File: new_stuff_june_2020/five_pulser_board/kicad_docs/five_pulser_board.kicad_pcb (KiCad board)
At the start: 2 copper layers, 39.4 x 78.7 mm, 49 parts, among them J1 signal_in, J2 CV_in, J3 Conn_02x05_Odd_Even, J4 signal_out, J5 pulses, U1 TL072, U2 LM3914, U3 TL072

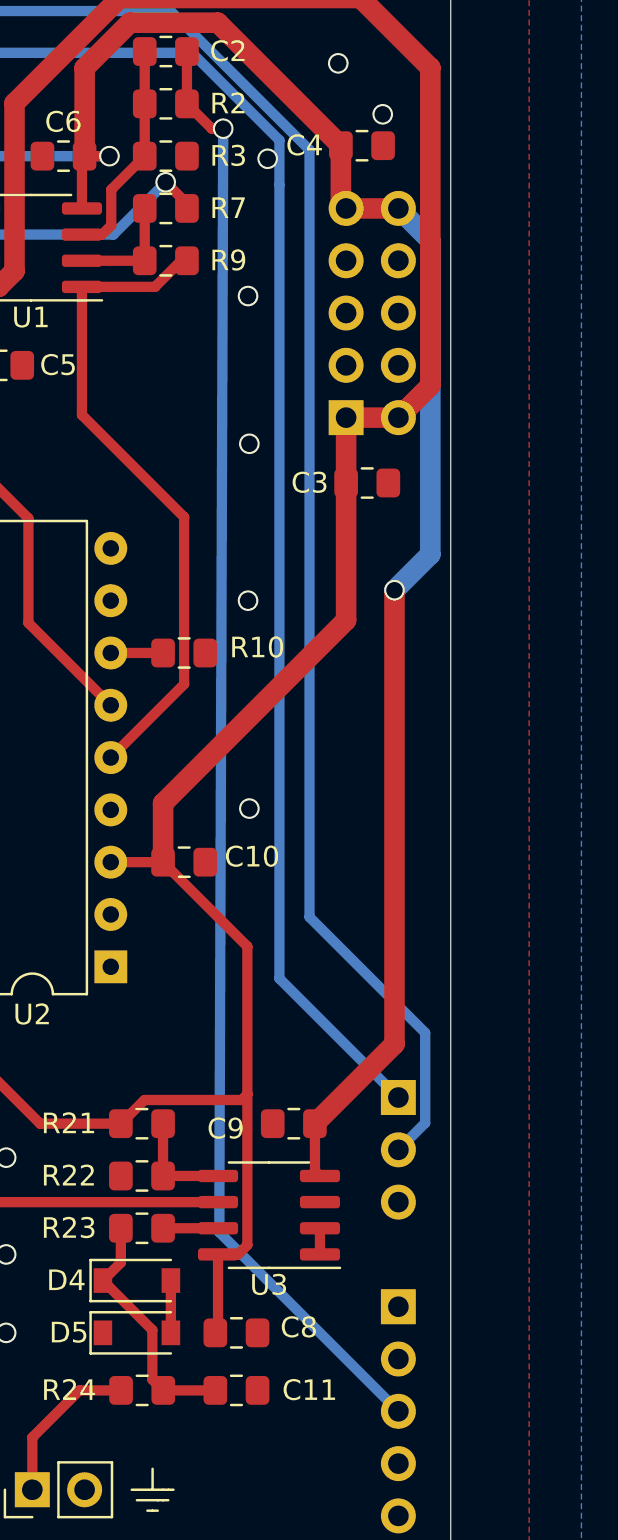
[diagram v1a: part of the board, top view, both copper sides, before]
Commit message: fix pcb error, change some values
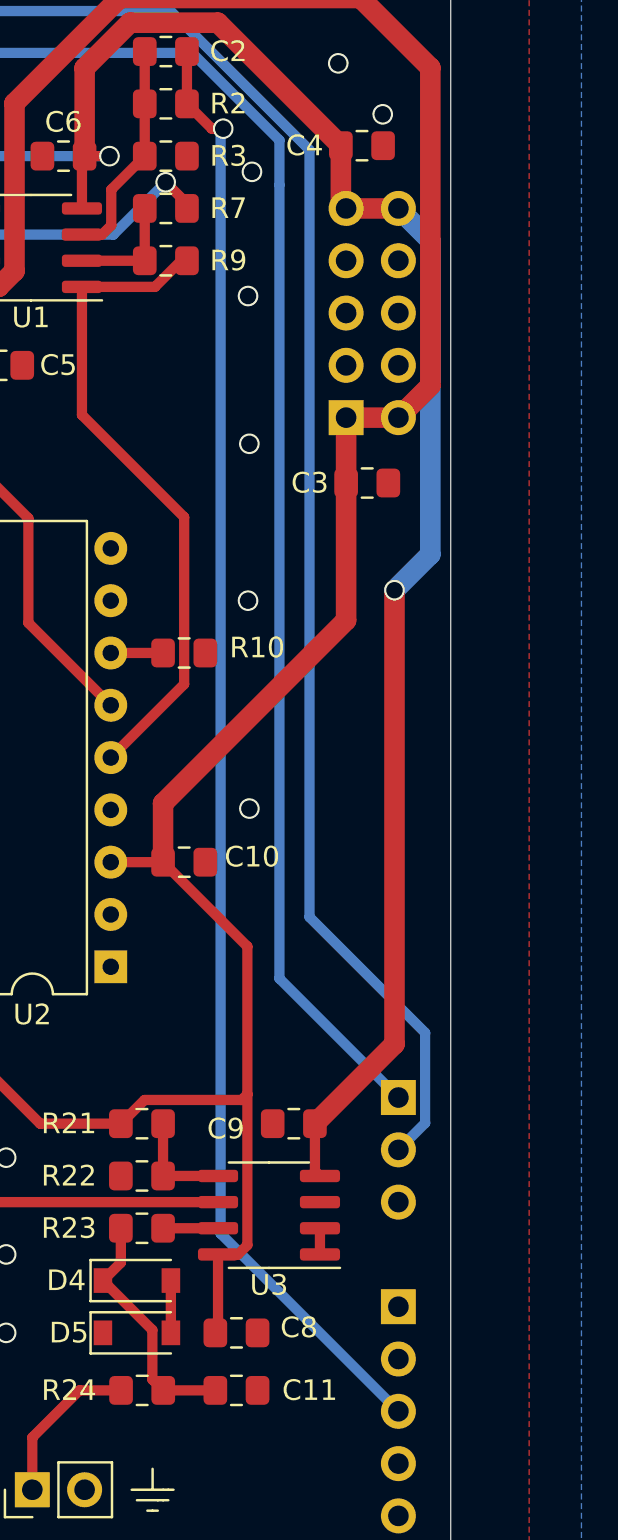
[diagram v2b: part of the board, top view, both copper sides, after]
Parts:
- C7: value 56pF -> 100nF
- R2, R7: value 220k -> 100k
- R3, R9: value 22k -> 10k
- R4: value 200k -> 100k
- R5, R6, R8: value 82k -> 100k

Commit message: scale pwm circuit and add power flags
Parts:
- R8: value 100k -> 39k
